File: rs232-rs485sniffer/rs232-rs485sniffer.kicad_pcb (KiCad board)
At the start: 2 copper layers, 42.4 x 50 mm, 15 parts, among them J1 supply, J2 USB_B, U1 MAX232, U2 MAX485E, U4 AMS1117-5.0

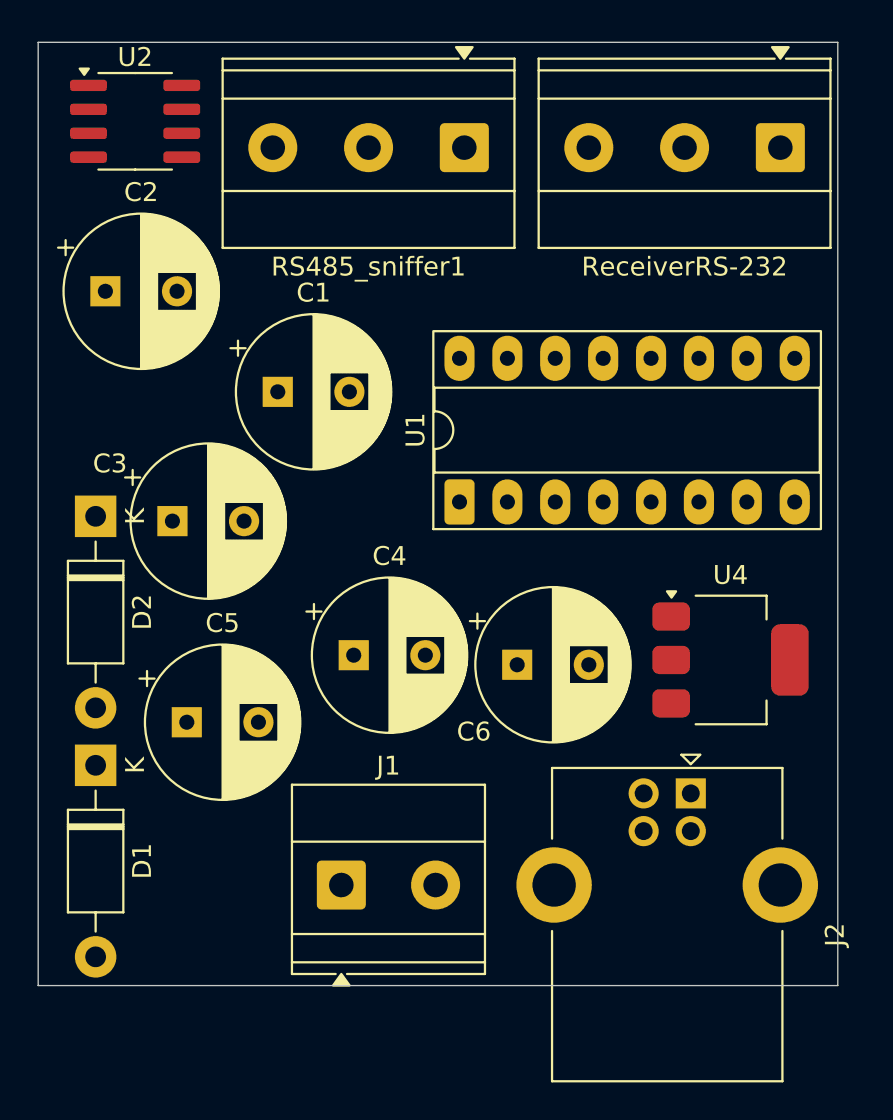
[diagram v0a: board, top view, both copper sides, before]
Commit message: [FIX] Add complete board v1 with gerber file
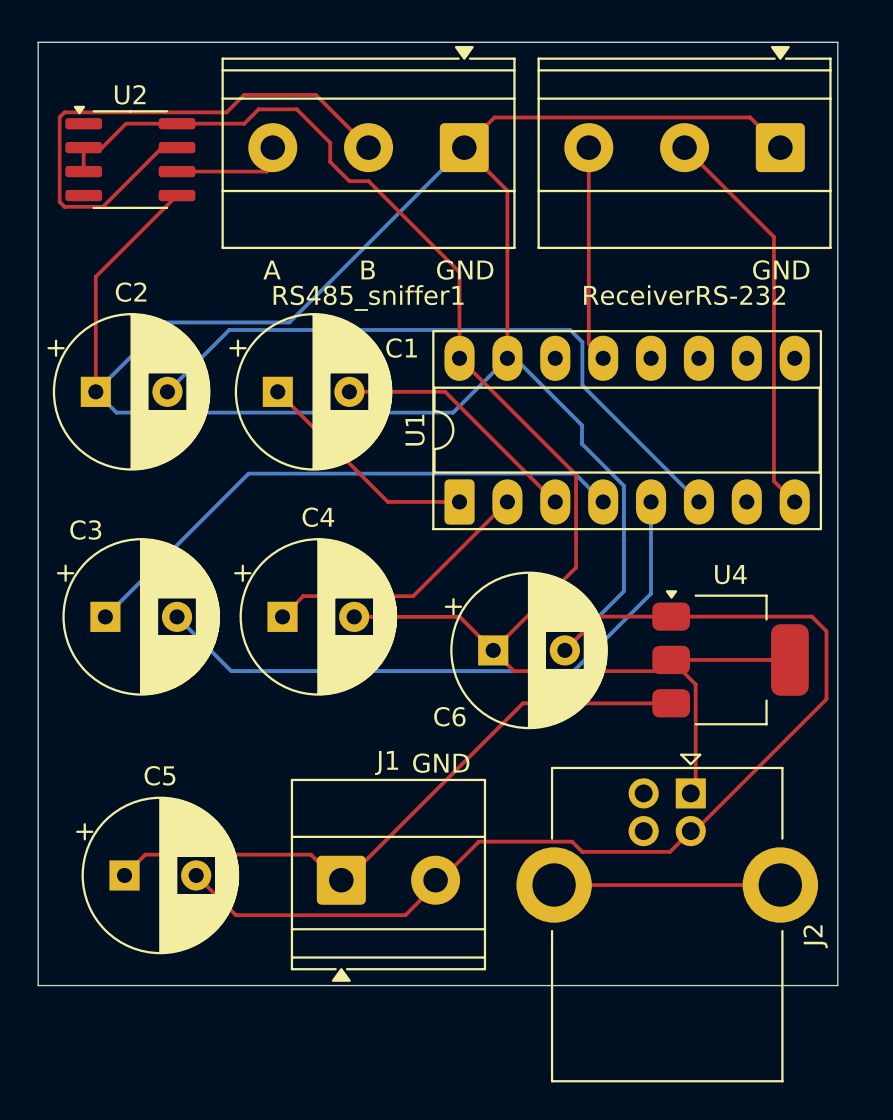
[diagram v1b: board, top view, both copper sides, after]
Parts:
- removed D1, D2: 1N4937, Diode_THT:D_DO-41_SOD81_P10.16mm_Horizontal
- moved C5 8.77 mm to (114.1, 95.0)
- moved C3 6.20 mm to (113.0, 81.3)
- moved C2 5.36 mm to (112.5, 69.3)
- moved C4 4.29 mm to (122.4, 81.3)
- moved U2 2.05 mm to (114.4, 57.0)
- moved C6 1.48 mm to (133.6, 83.1)
- moved J1 0.25 mm to (125.6, 95.2)
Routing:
- net GND: track 0.00 -> 168.4 mm
- net +5V: track 0.00 -> 82.9 mm
- net Net-(U1-VS-): track 0.00 -> 34.7 mm
- net Net-(J1-Pin_1): track 0.00 -> 34.1 mm
- net Net-(U1-C2-): track 0.00 -> 32.9 mm
- net Net-(U1-C2+): track 0.00 -> 30.2 mm
- net Net-(RS485_sniffer1-Pin_2): track 0.00 -> 30.2 mm
- net Net-(ReceiverRS-232-Pin_2): track 0.00 -> 21.2 mm
- net Net-(U1-VS+): track 0.00 -> 14.5 mm
- net Net-(U1-C1-): track 0.00 -> 13.3 mm
- net Net-(U1-C1+): track 0.00 -> 12.1 mm
- net unconnected-(J2-Shield-Pad5): track 0.00 -> 12.0 mm
- net Net-(ReceiverRS-232-Pin_3): track 0.00 -> 11.5 mm
- net Net-(RS485_sniffer1-Pin_3): track 0.00 -> 6.17 mm
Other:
- board text added: "A"
- board text added: "B"
- board text added: "GND"

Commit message: [ADD] Add 2 resistor to moderate signal of TTL
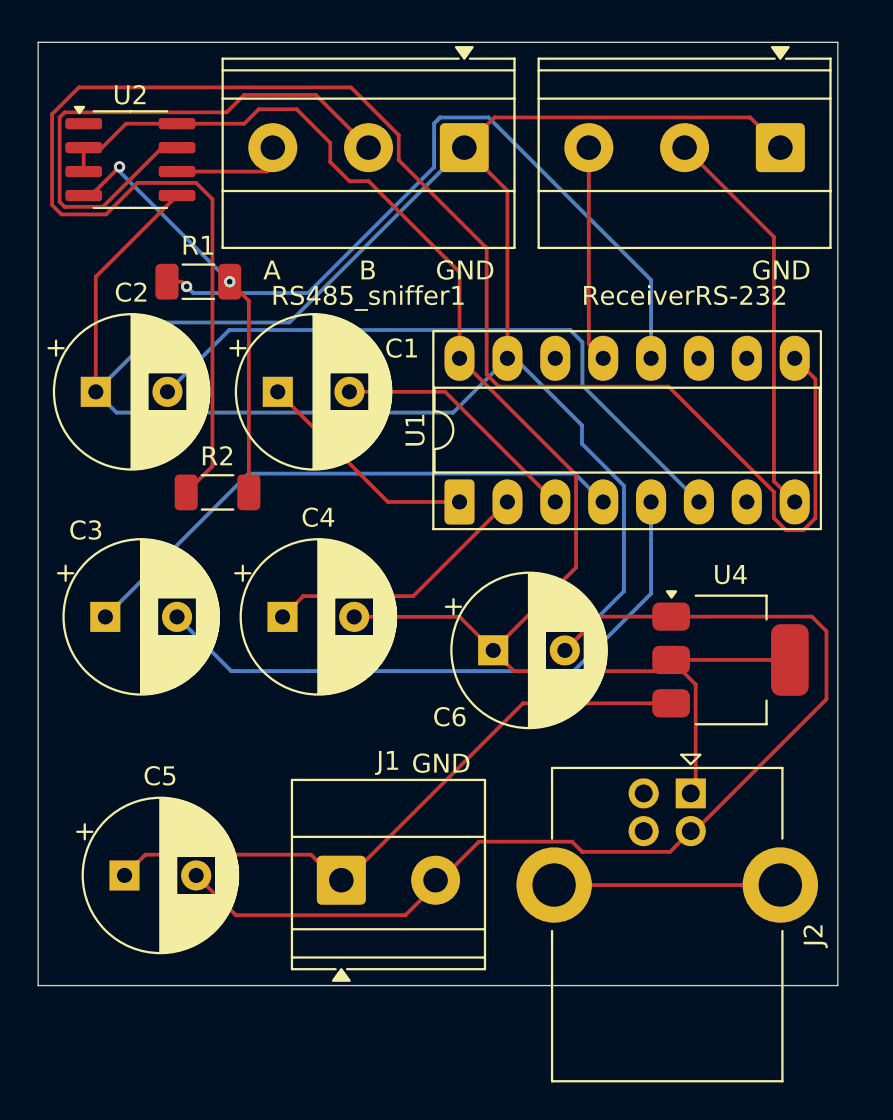
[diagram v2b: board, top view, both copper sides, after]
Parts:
- added R1: 1k, Inductor_SMD:L_1206_3216Metric_Pad1.22x1.90mm_HandSolder, F.Cu at (118.0, 63.5)
- added R2: 1k, Inductor_SMD:L_1206_3216Metric_Pad1.22x1.90mm_HandSolder, F.Cu at (119.0, 74.7)
- J1: value supply -> supply pin 5 GND pin 9 +12V
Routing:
- net Net-(U1-R2OUT): track 0.00 -> 96.2 mm
- net Net-(U1-R1OUT): track 0.00 -> 38.9 mm, vias 0 -> 1
- net Net-(U2-DI): track 0.00 -> 22.6 mm, vias 0 -> 2
